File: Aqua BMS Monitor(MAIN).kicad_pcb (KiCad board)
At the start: 4 copper layers, 130.2 x 96.2 mm, 246 parts, among them J1 UART Jpins, J2 XT60PW-M, J3 XT60PW-M, J4 XT60PW-M, J5 SWD_01x04_Pin, J6 XT60PW-M, J7 USB_C_Female_USB2_Small, Q6 NPN, U1 BQ7695202, U2 STM32F205RETx, U4 LM66100DCKR, U5 LM66100DCKR, U6 LM66100DCKR, U7 LTC4359-DCB, U9 AMS1117-3.3, X1 X322516MRB4SI

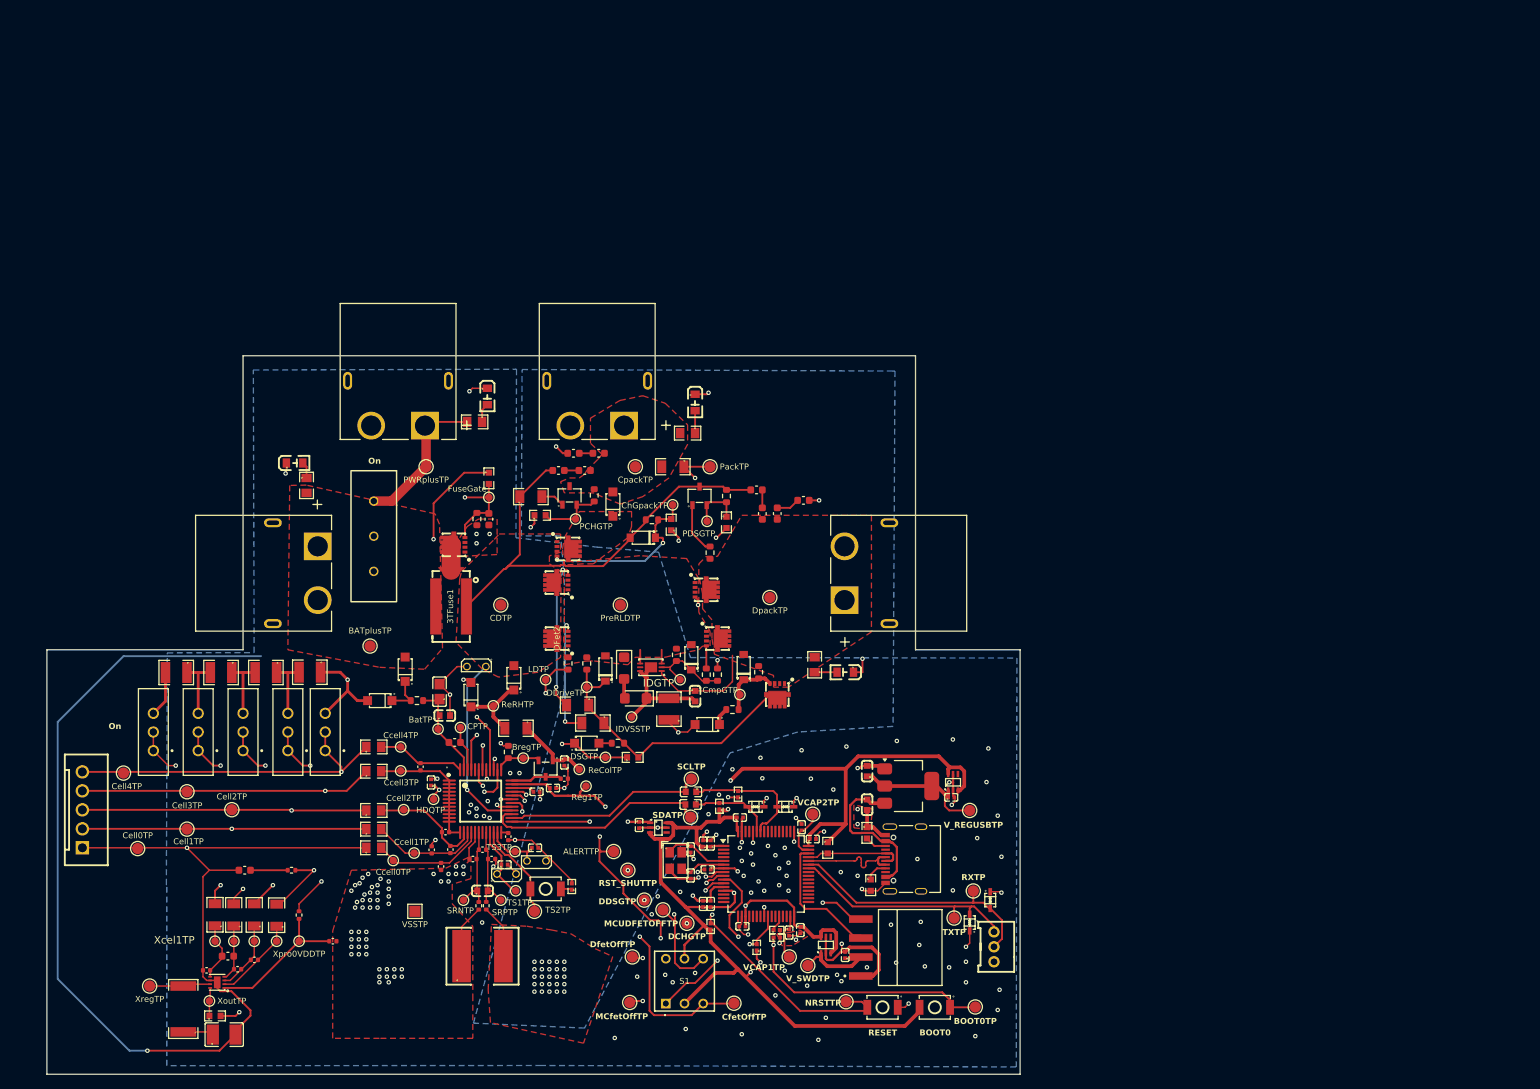
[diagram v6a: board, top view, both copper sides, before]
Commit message: Added gaping holes
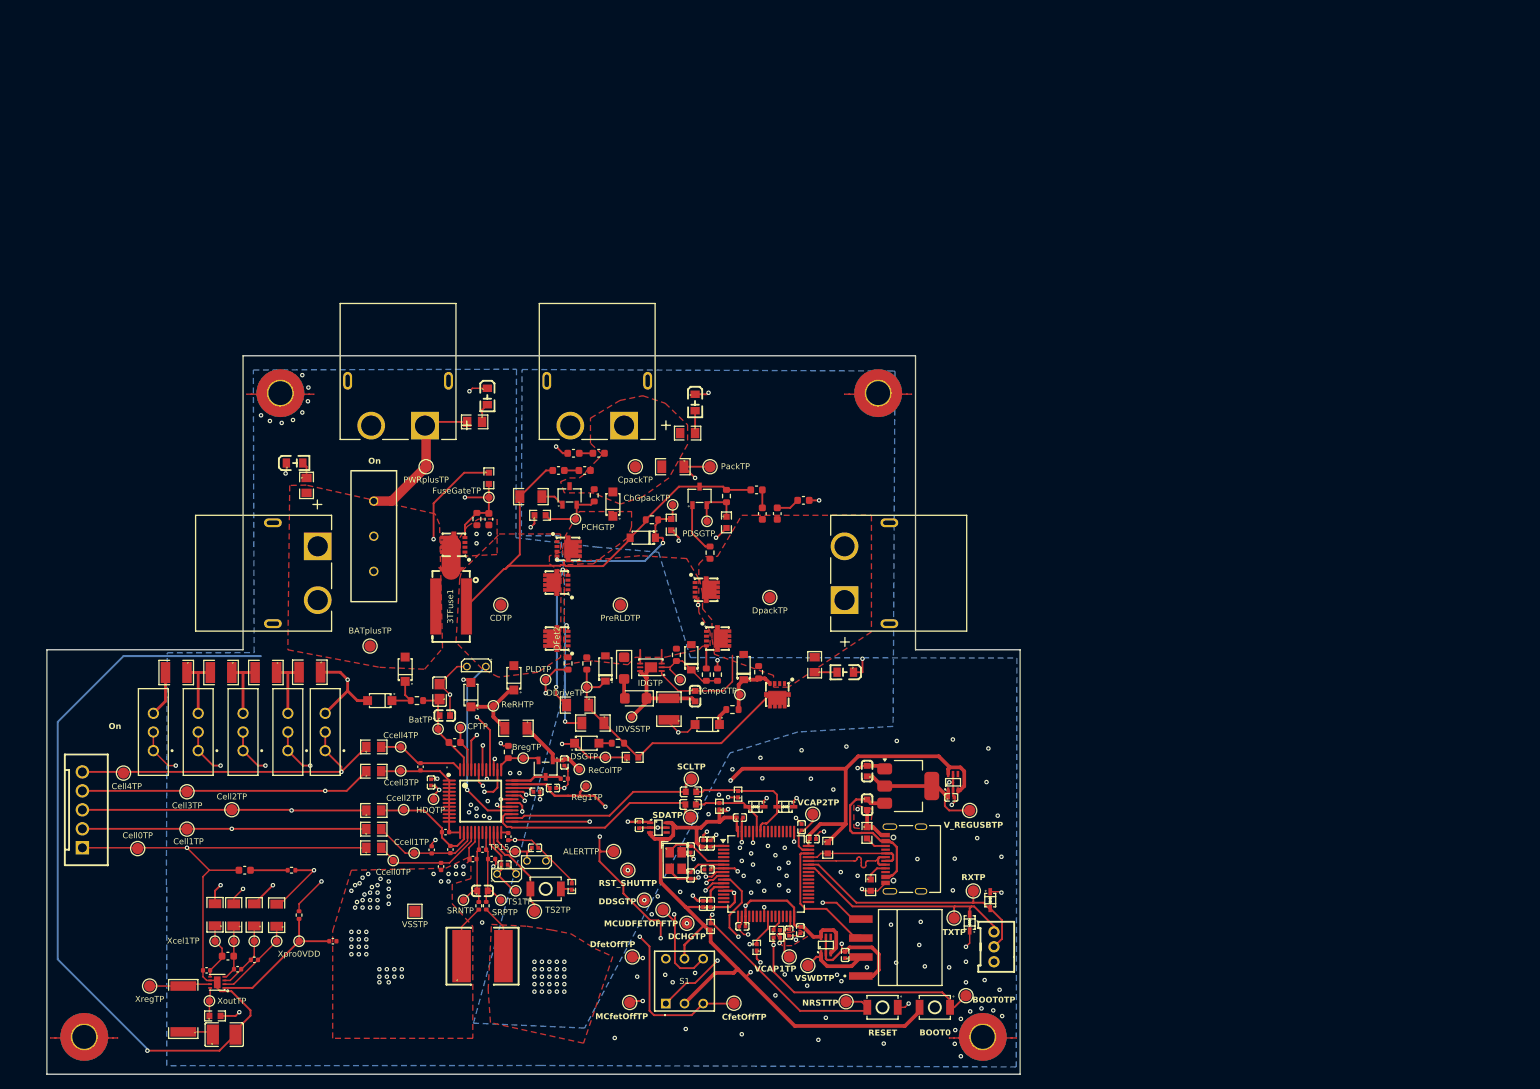
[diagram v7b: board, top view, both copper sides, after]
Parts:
- added H1: MountingHole_Pad, MountingHole:MountingHole_3.2mm_M3_Pad_TopBottom, F.Cu at (102.0, 68.2)
- added H2: MountingHole_Pad, MountingHole:MountingHole_3.2mm_M3_Pad_TopBottom, F.Cu at (182.0, 68.2)
- added H3: MountingHole_Pad, MountingHole:MountingHole_3.2mm_M3_Pad_TopBottom, F.Cu at (75.8, 154.4)
- added H4: MountingHole_Pad, MountingHole:MountingHole_3.2mm_M3_Pad_TopBottom, F.Cu at (196.0, 154.4)
- PdR2: value R 10M -> 10M
- TP27: value FuseGate -> FuseGateTP
- TP37: value Xpro0VDDTP -> Xpro0VDD
- TP51: value LDTP -> PLDTP
- moved TP64 1.96 mm to (193.8, 148.8)
- renumbered TS3TP to TP15, V_SWDTP to VSWDTP
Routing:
- net BAT-: track 316.4 -> 315.0 mm, vias 171 -> 187
- net Net-(U2-BOOT0): track 51.3 -> 50.1 mm

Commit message: Changes to mounting points and gnd path
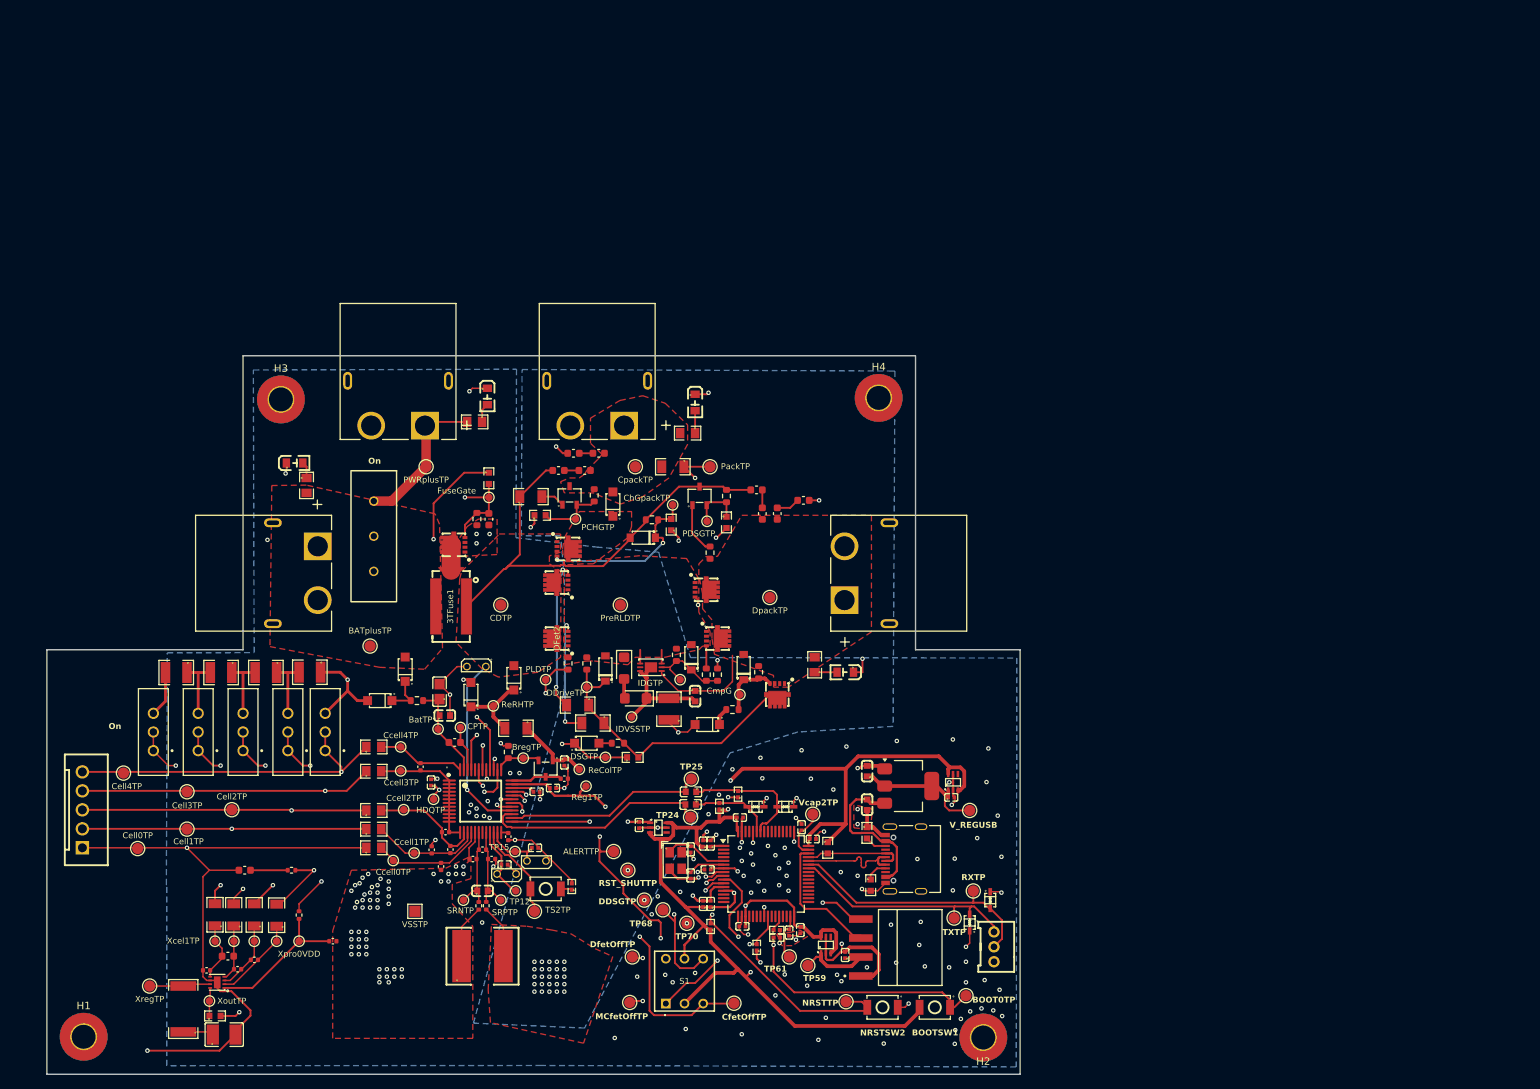
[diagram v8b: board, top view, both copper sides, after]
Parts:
- TP27: value FuseGateTP -> FuseGate
- TP53: value CmpGTP -> CmpG
- TP60: value V_REGUSBTP -> V_REGUSB
- TP62: value VCAP2TP -> Vcap2TP
- moved H1 90.1 mm to (75.7, 154.3)
- moved H3 89.3 mm to (102.1, 69.0)
- moved H2 87.4 mm to (196.1, 154.4)
- moved H4 86.6 mm to (182.1, 68.8)
- renumbered BOOT0 to BOOTSW1, RESET to NRSTSW2, TS1TP to TP12, SDATP to TP24, SCLTP to TP25, VSWDTP to TP59, VCAP1TP to TP61, MCUDFETOFFTP to TP68, DCHGTP to TP70
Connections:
- H1 pad 1: BAT- -> unconnected-(H1-Pad1)
- H2 pad 1: BAT- -> unconnected-(H2-Pad1)
- H3 pad 1: BAT- -> unconnected-(H3-Pad1)_1
- H4 pad 1: BAT- -> unconnected-(H4-Pad1)_1
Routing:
- net BAT-: track 315.0 -> 332.7 mm, vias 187 -> 179
